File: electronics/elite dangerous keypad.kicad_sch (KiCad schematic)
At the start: 10 parts, among them SW1 SW_SPST, U1 MCP23018x-x-SP, U2 MCP23018x-x-SP

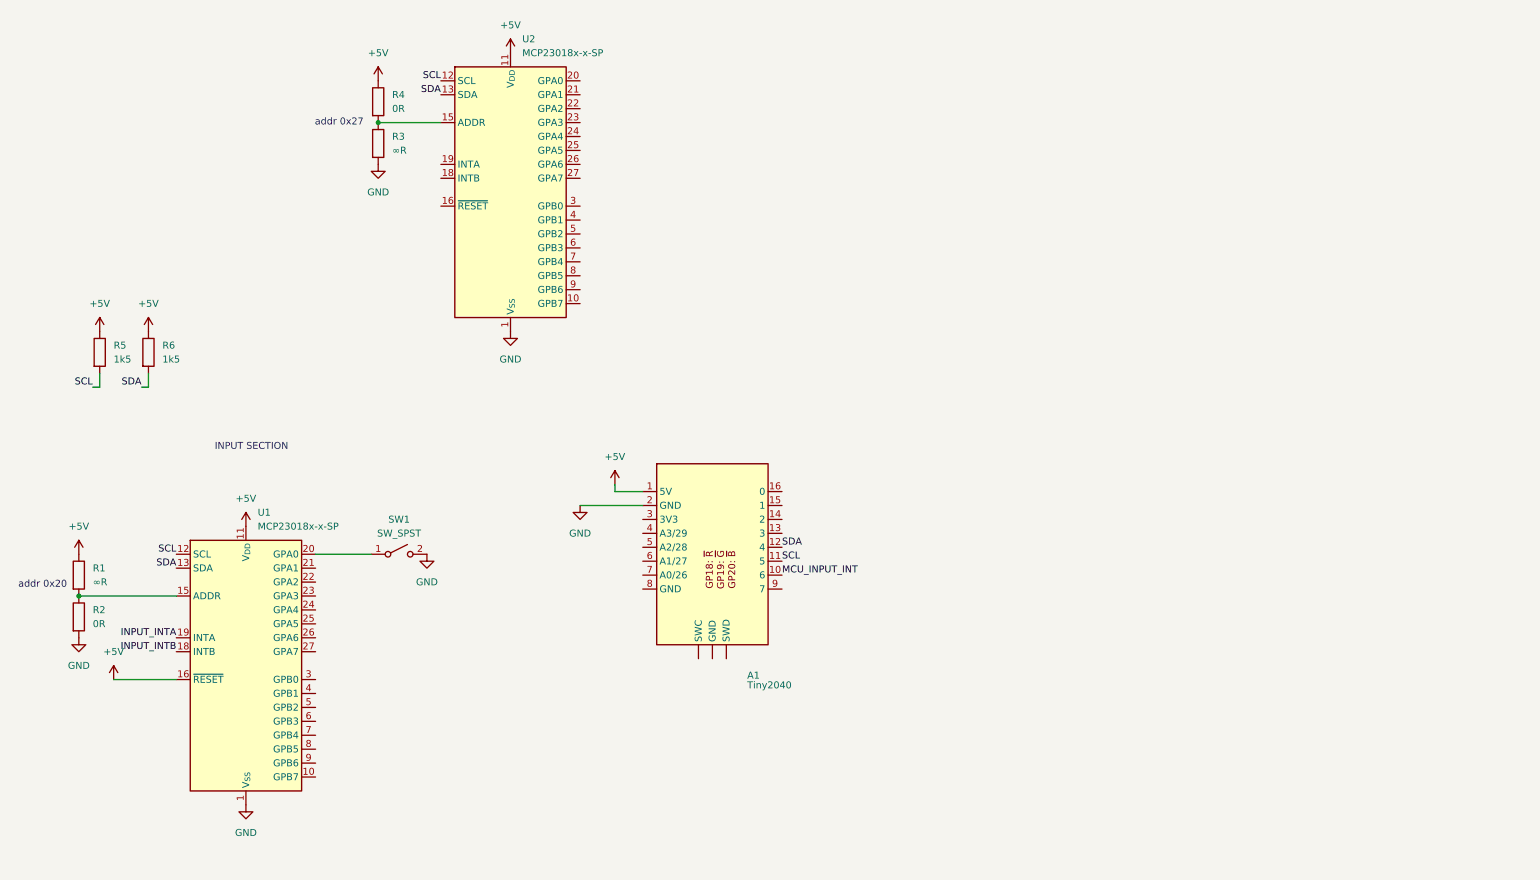
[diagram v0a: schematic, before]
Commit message: schematic for cardboard box version
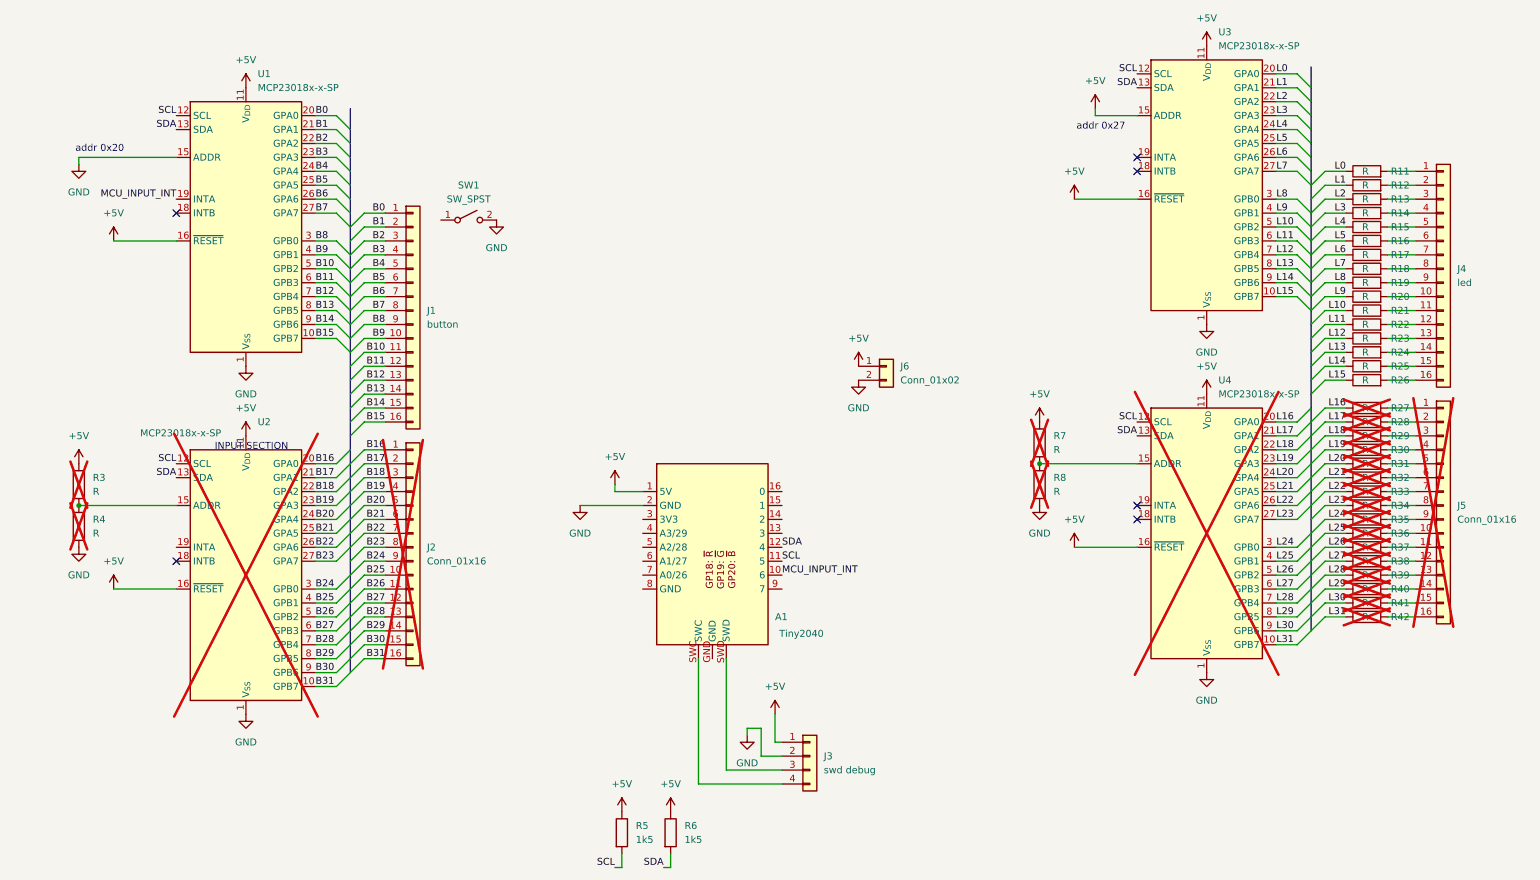
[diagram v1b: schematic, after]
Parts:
- removed R1: ∞R, symbol Device:R
- removed R2: 0R, symbol Device:R
- added J1: button, Connector_PinHeader_2.54mm:PinHeader_1x16_P2.54mm_Vertical, symbol Connector_Generic:Conn_01x16
- added J2, J5: Conn_01x16, Connector_PinHeader_2.54mm:PinHeader_1x16_P2.54mm_Vertical, symbol Connector_Generic:Conn_01x16
- added J3: swd debug, Connector_PinHeader_2.54mm:PinHeader_1x04_P2.54mm_Vertical, symbol Connector_Generic:Conn_01x04
- added J4: led, Connector_PinHeader_2.54mm:PinHeader_1x16_P2.54mm_Vertical, symbol Connector_Generic:Conn_01x16
- added J6: Conn_01x02, Connector_PinSocket_2.54mm:PinSocket_1x02_P2.54mm_Vertical, symbol Connector_Generic:Conn_01x02
- added R11, R12, R13, R14, R15, R16, R17, R18, R19, R20, R21, R22, R23, R24, R25, R26: R, Resistor_THT:R_Axial_DIN0204_L3.6mm_D1.6mm_P7.62mm_Horizontal, symbol Device:R
- added R27, R28, R29, R30, R31, R32, R33, R34, R35, R36, R37, R38, R39, R40, R41, R42: R, symbol Device:R
- added R7, R8: R, Resistor_THT:R_Axial_DIN0204_L3.6mm_D1.6mm_P2.54mm_Vertical, symbol Device:R
- added U2, U4: MCP23018x-x-SP, Package_DIP:DIP-28_W7.62mm, symbol Interface_Expansion:MCP23018x-x-SP
- R3: value ∞R -> R; footprint (none) -> Resistor_THT:R_Axial_DIN0204_L3.6mm_D1.6mm_P2.54mm_Vertical; now not fitted
- R4: value 0R -> R; footprint (none) -> Resistor_THT:R_Axial_DIN0204_L3.6mm_D1.6mm_P2.54mm_Vertical; now not fitted
- R5, R6: footprint (none) -> Resistor_THT:R_Axial_DIN0204_L3.6mm_D1.6mm_P2.54mm_Vertical
- renumbered U2 to U3
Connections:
- net INPUT_INTA is gone; now on net MCU_INPUT_INT: U1.19 (INTA)
- net +5V: now also R3.1, U3.15 (ADDR), U3.16 (~{RESET}), J3.1 (Pin_1), J6.1 (Pin_1), R7.1, U2.11 (V_{DD}), U2.16 (~{RESET}), U4.11 (V_{DD}), U4.16 (~{RESET}); no longer R4.1
- net GND: now also R4.2, U1.15 (ADDR), J3.2 (Pin_2), J6.2 (Pin_2), R8.2, U2.1 (V_{SS}), U4.1 (V_{SS}); no longer R3.2
- net SCL: now also U2.12 (SCL), U4.12 (SCL)
- net SDA: now also U2.13 (SDA), U4.13 (SDA)
- net L15: now reaches U3.10 (GPB7)
- net L15: now also R26.1
- net L0: now reaches U3.20 (GPA0)
- net L0: now also R11.1
- net L1: now reaches U3.21 (GPA1)
- net L1: now also R12.1
- net L2: now reaches U3.22 (GPA2)
- net L2: now also R13.1
- net L3: now reaches U3.23 (GPA3)
- net L3: now also R14.1
- net L4: now reaches U3.24 (GPA4)
- net L4: now also R15.1
- net L5: now reaches U3.25 (GPA5)
- net L5: now also R16.1
- net L6: now reaches U3.26 (GPA6)
- net L6: now also R17.1
- net L7: now reaches U3.27 (GPA7)
- net L7: now also R18.1
- net L8: now reaches U3.3 (GPB0)
- net L8: now also R19.1
- net L9: now reaches U3.4 (GPB1)
- net L9: now also R20.1
- net L10: now reaches U3.5 (GPB2)
- net L10: now also R21.1
- net L11: now reaches U3.6 (GPB3)
- net L11: now also R22.1
- net L12: now reaches U3.7 (GPB4)
- net L12: now also R23.1
- net L13: now reaches U3.8 (GPB5)
- net L13: now also R24.1
- net L14: now reaches U3.9 (GPB6)
- net L14: now also R25.1
- net B15: now reaches U1.10 (GPB7)
- net B15: now also J1.16 (Pin_16)
- net at SW1.1 (A): no longer U1.20 (GPA0)
- net B1: now reaches U1.21 (GPA1)
- net B1: now also J1.2 (Pin_2)
- net B2: now reaches U1.22 (GPA2)
- net B2: now also J1.3 (Pin_3)
- net B3: now reaches U1.23 (GPA3)
- net B3: now also J1.4 (Pin_4)
- net B4: now reaches U1.24 (GPA4)
- net B4: now also J1.5 (Pin_5)
- net B5: now reaches U1.25 (GPA5)
- net B5: now also J1.6 (Pin_6)
- net B6: now reaches U1.26 (GPA6)
- net B6: now also J1.7 (Pin_7)
- net B7: now reaches U1.27 (GPA7)
- net B7: now also J1.8 (Pin_8)
- net B8: now reaches U1.3 (GPB0)
- net B8: now also J1.9 (Pin_9)
- net B9: now reaches U1.4 (GPB1)
- net B9: now also J1.10 (Pin_10)
- net B10: now reaches U1.5 (GPB2)
- net B10: now also J1.11 (Pin_11)
- net B11: now reaches U1.6 (GPB3)
- net B11: now also J1.12 (Pin_12)
- net B12: now reaches U1.7 (GPB4)
- net B12: now also J1.13 (Pin_13)
- net B13: now reaches U1.8 (GPB5)
- net B13: now also J1.14 (Pin_14)
- net B14: now reaches U1.9 (GPB6)
- net B14: now also J1.15 (Pin_15)
- net INPUT_INTB: no longer names the net of U1.18 (INTB)
- new net: J5.3 (Pin_3), R29.2
- new net: J5.14 (Pin_14), R40.2
- new net: R3.2, R4.1, U2.15 (ADDR)
- new net: J4.14 (Pin_14), R24.2
- new net: J4.15 (Pin_15), R25.2
- new net: J5.11 (Pin_11), R37.2
- new net: J4.7 (Pin_7), R17.2
- new net: J5.1 (Pin_1), R27.2
- new net: J5.10 (Pin_10), R36.2
- new net: J5.12 (Pin_12), R38.2
- new net: J5.13 (Pin_13), R39.2
- new net: J5.15 (Pin_15), R41.2
- new net: J5.16 (Pin_16), R42.2
- new net: J5.2 (Pin_2), R28.2
- new net: J5.4 (Pin_4), R30.2
- new net: J5.5 (Pin_5), R31.2
- new net: J5.6 (Pin_6), R32.2
- new net: J5.7 (Pin_7), R33.2
- new net: J5.8 (Pin_8), R34.2
- new net: J5.9 (Pin_9), R35.2
- new net: J4.3 (Pin_3), R13.2
- new net: J4.12 (Pin_12), R22.2
- new net: J4.10 (Pin_10), R20.2
- new net: J4.13 (Pin_13), R23.2
- new net: J4.9 (Pin_9), R19.2
- new net: J4.5 (Pin_5), R15.2
- new net: R7.2, R8.1, U4.15 (ADDR)
- new net: J4.4 (Pin_4), R14.2
- new net: J4.1 (Pin_1), R11.2
- new net: J4.11 (Pin_11), R21.2
- new net: J4.16 (Pin_16), R26.2
- new net: J4.2 (Pin_2), R12.2
- new net: J4.6 (Pin_6), R16.2
- new net: J4.8 (Pin_8), R18.2
- new net: A1.SWC, J3.4 (Pin_4)
- new net: A1.SWD, J3.3 (Pin_3)
- new net B0: J1.1 (Pin_1), U1.20 (GPA0)
- new net B16: J2.1 (Pin_1), U2.20 (GPA0)
- new net B17: J2.2 (Pin_2), U2.21 (GPA1)
- new net B18: J2.3 (Pin_3), U2.22 (GPA2)
- new net B19: J2.4 (Pin_4), U2.23 (GPA3)
- new net B20: J2.5 (Pin_5), U2.24 (GPA4)
- new net B21: J2.6 (Pin_6), U2.25 (GPA5)
- new net B22: J2.7 (Pin_7), U2.26 (GPA6)
- new net B23: J2.8 (Pin_8), U2.27 (GPA7)
- new net B24: J2.9 (Pin_9), U2.3 (GPB0)
- new net B25: J2.10 (Pin_10), U2.4 (GPB1)
- new net B26: J2.11 (Pin_11), U2.5 (GPB2)
- new net B27: J2.12 (Pin_12), U2.6 (GPB3)
- new net B28: J2.13 (Pin_13), U2.7 (GPB4)
- new net B29: J2.14 (Pin_14), U2.8 (GPB5)
- new net B30: J2.15 (Pin_15), U2.9 (GPB6)
- new net B31: J2.16 (Pin_16), U2.10 (GPB7)
- new net L16: R27.1, U4.20 (GPA0)
- new net L17: R28.1, U4.21 (GPA1)
- new net L18: R29.1, U4.22 (GPA2)
- new net L19: R30.1, U4.23 (GPA3)
- new net L20: R31.1, U4.24 (GPA4)
- new net L21: R32.1, U4.25 (GPA5)
- new net L22: R33.1, U4.26 (GPA6)
- new net L23: R34.1, U4.27 (GPA7)
- new net L24: R35.1, U4.3 (GPB0)
- new net L25: R36.1, U4.4 (GPB1)
- new net L26: R37.1, U4.5 (GPB2)
- new net L27: R38.1, U4.6 (GPB3)
- new net L28: R39.1, U4.7 (GPB4)
- new net L29: R40.1, U4.8 (GPB5)
- new net L30: R41.1, U4.9 (GPB6)
- new net L31: R42.1, U4.10 (GPB7)
- no-connect marks 0 -> 6
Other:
- moved on the sheet: R5, R6, SW1, U1, U3

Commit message: feat(electronics): quadrature schematic
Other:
- added sheet KY-040 rotary encoder (KY-040.kicad_sch)

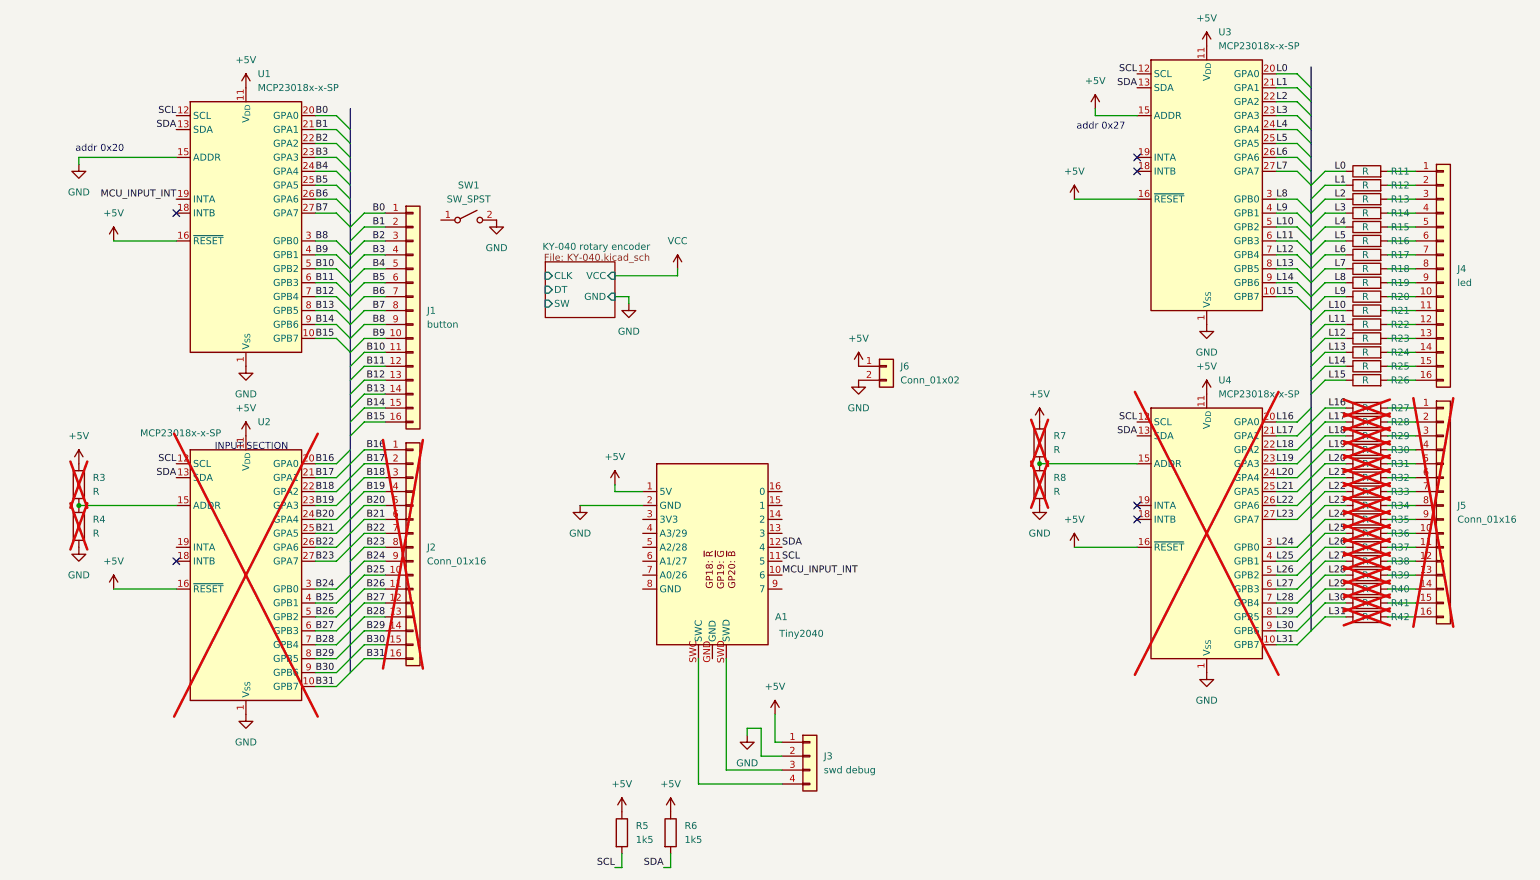
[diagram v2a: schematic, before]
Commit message: docs(electronics): reformat for readability
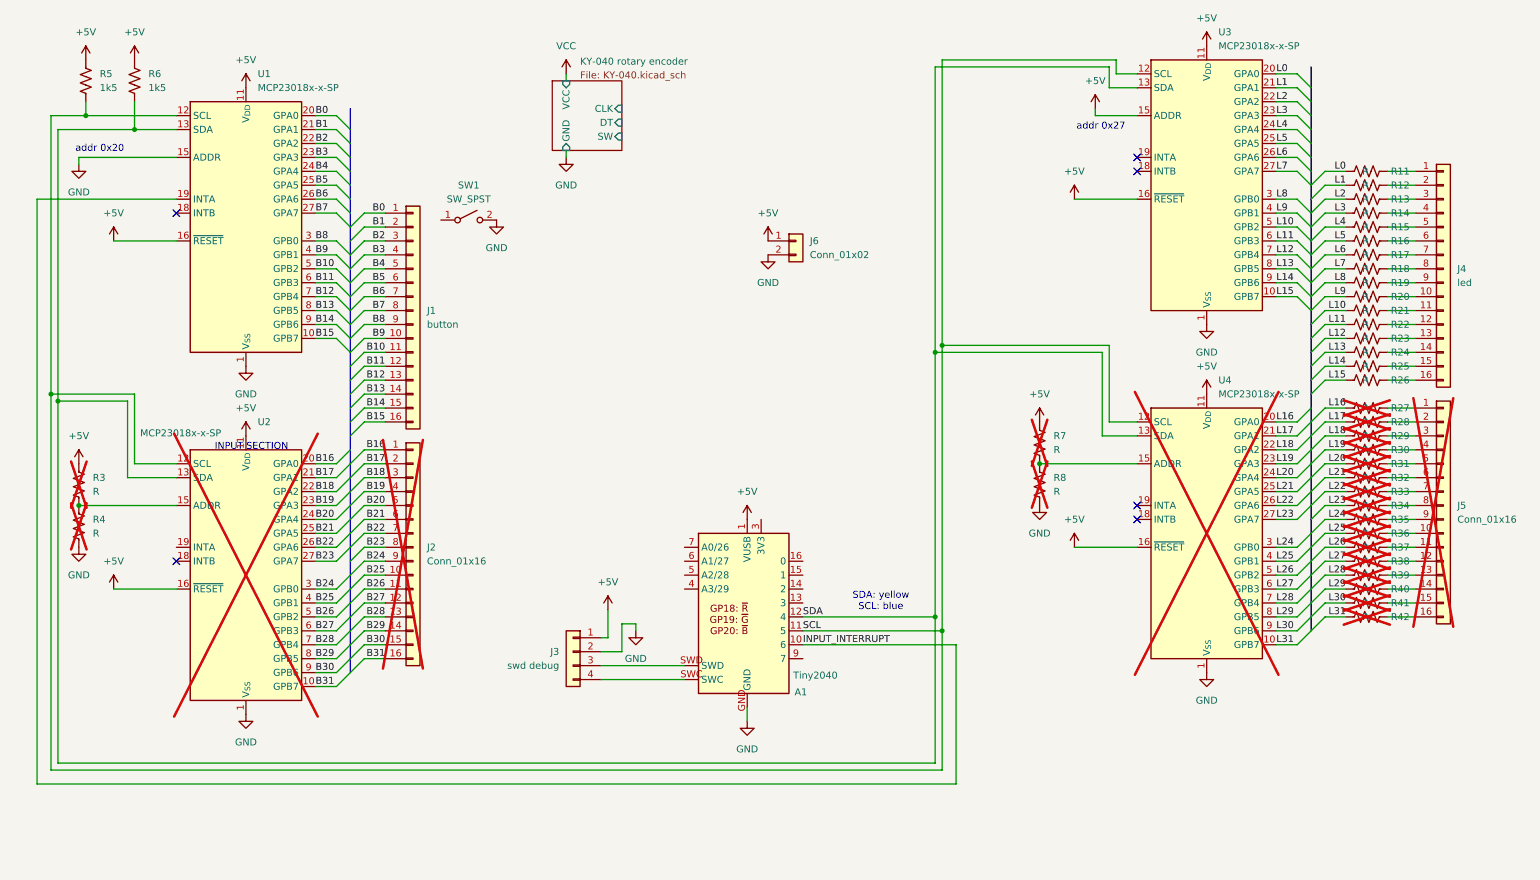
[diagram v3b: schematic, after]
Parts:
- R11, R12, R13, R14, R15, R16, R17, R18, R19, R20, R21, R22, R23, R24, R25, R26, R27, R28, R29, R3, R30, R31, R32, R33, R34, R35, R36, R37, R38, R39, R4, R40, R41, R42, R5, R6, R7, R8: symbol Device:R -> Device:R_US
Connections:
- net GND: now also A1.8 (GND), A1.GND
- net MCU_INPUT_INT renamed INPUT_INTERRUPT
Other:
- note added: "SDA: yellow SCL: blue"
- moved on the sheet: J3, J6
